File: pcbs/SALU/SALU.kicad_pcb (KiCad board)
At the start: 4 copper layers, 13 parts, among them J201 Conn_02x20_Odd_Even, U201 74HC245, U202 74HC245

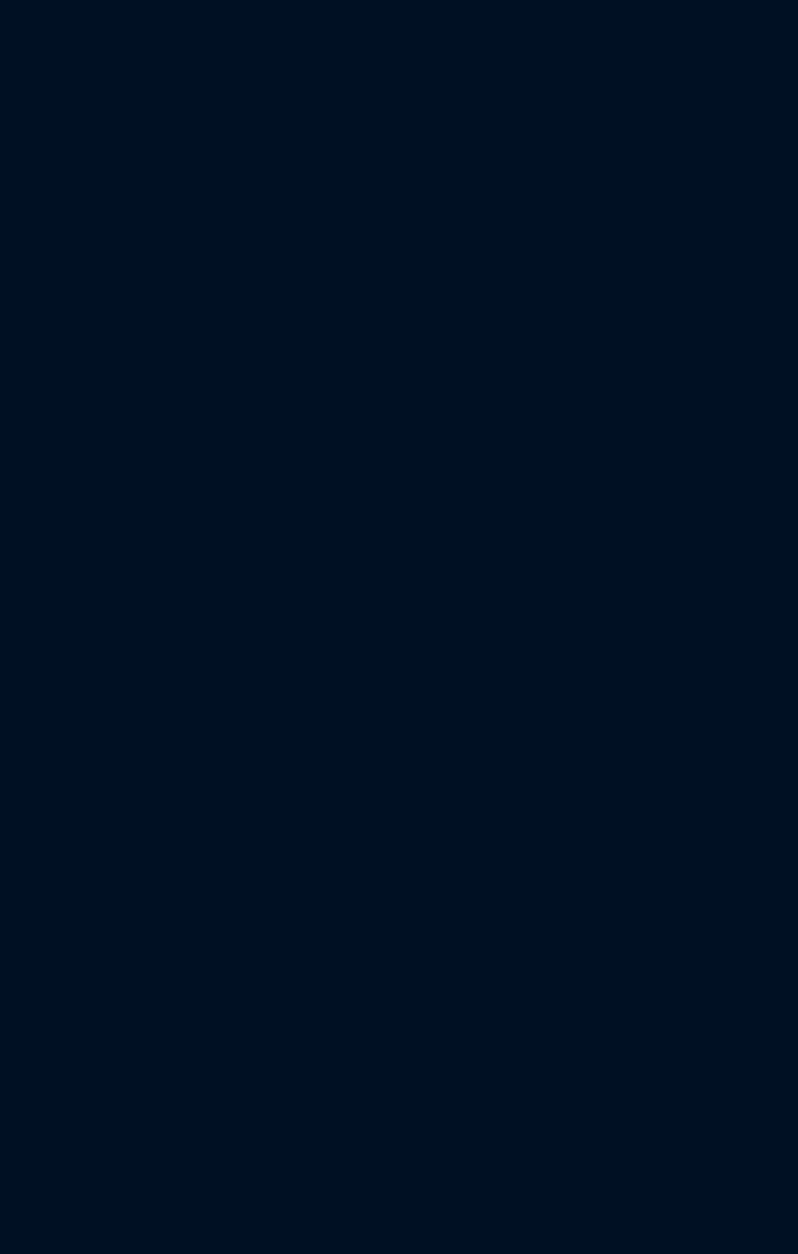
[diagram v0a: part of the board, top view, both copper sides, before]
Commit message: Decoder stage
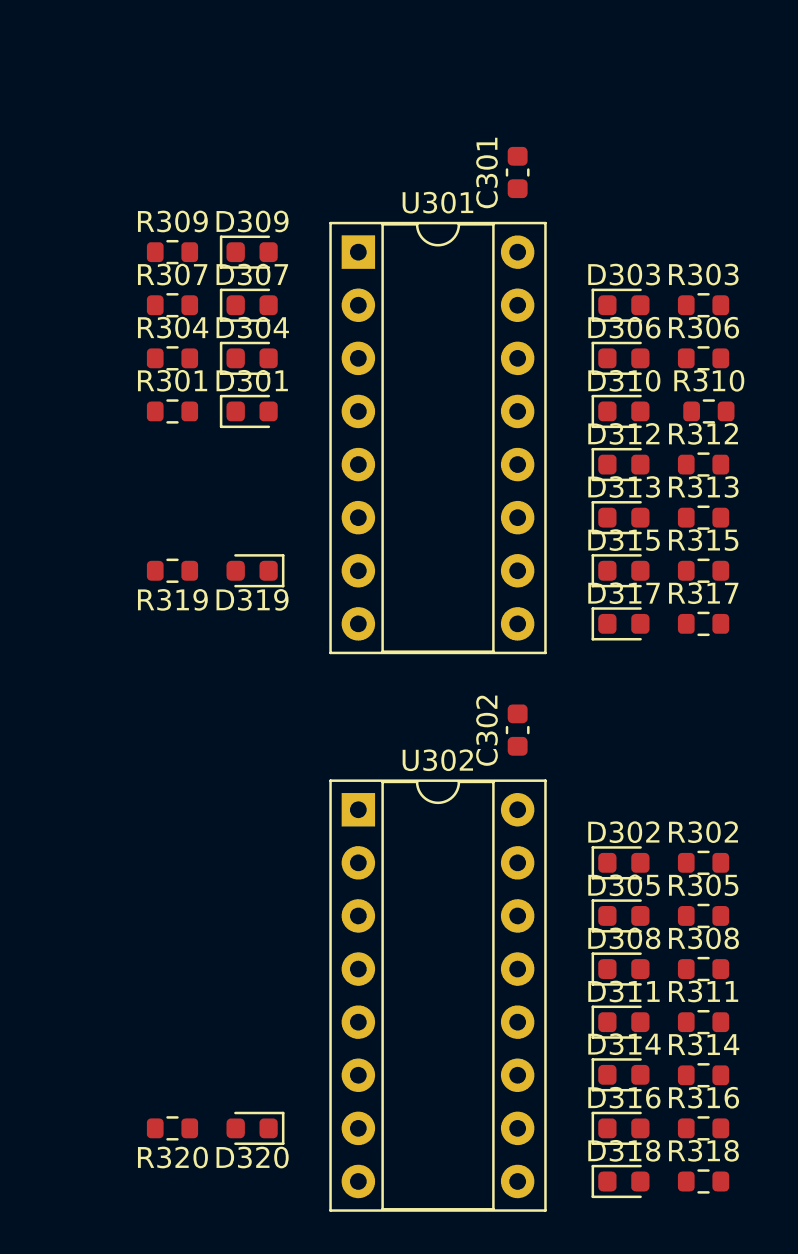
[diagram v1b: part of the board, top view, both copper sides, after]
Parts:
- added C301: 100n, Capacitor_SMD:C_0603_1608Metric, F.Cu at (66.0, 120.7)
- added C302: 100n, Capacitor_SMD:C_0603_1608Metric, F.Cu at (66.0, 147.3)
- added D301: GREEN, LED_SMD:LED_0603_1608Metric, F.Cu at (53.3, 132.1)
- added D302: GREEN, LED_SMD:LED_0603_1608Metric, F.Cu at (71.1, 153.7)
- added D303: GREEN, LED_SMD:LED_0603_1608Metric, F.Cu at (71.1, 127.0)
- added D304: GREEN, LED_SMD:LED_0603_1608Metric, F.Cu at (53.3, 129.5)
- added D305: GREEN, LED_SMD:LED_0603_1608Metric, F.Cu at (71.1, 156.2)
- added D306: GREEN, LED_SMD:LED_0603_1608Metric, F.Cu at (71.1, 129.5)
- added D307: GREEN, LED_SMD:LED_0603_1608Metric, F.Cu at (53.3, 127.0)
- added D308: RED, LED_SMD:LED_0603_1608Metric, F.Cu at (71.1, 158.8)
- added D309: GREEN, LED_SMD:LED_0603_1608Metric, F.Cu at (53.3, 124.5)
- added D310: GREEN, LED_SMD:LED_0603_1608Metric, F.Cu at (71.1, 132.1)
- added D311: RED, LED_SMD:LED_0603_1608Metric, F.Cu at (71.1, 161.3)
- added D312: GREEN, LED_SMD:LED_0603_1608Metric, F.Cu at (71.1, 134.6)
- added D313: RED, LED_SMD:LED_0603_1608Metric, F.Cu at (71.1, 137.2)
- added D314: GREEN, LED_SMD:LED_0603_1608Metric, F.Cu at (71.1, 163.8)
- added D315: RED, LED_SMD:LED_0603_1608Metric, F.Cu at (71.1, 139.7)
- added D316: GREEN, LED_SMD:LED_0603_1608Metric, F.Cu at (71.1, 166.4)
- added D317: RED, LED_SMD:LED_0603_1608Metric, F.Cu at (71.1, 142.2)
- added D318: GREEN, LED_SMD:LED_0603_1608Metric, F.Cu at (71.1, 168.9)
- added D319: RED, LED_SMD:LED_0603_1608Metric, F.Cu at (53.3, 139.7)
- added D320: GREEN, LED_SMD:LED_0603_1608Metric, F.Cu at (53.3, 166.4)
- added R301: 4k7, Resistor_SMD:R_0603_1608Metric, F.Cu at (49.5, 132.1)
- added R302: 4k7, Resistor_SMD:R_0603_1608Metric, F.Cu at (74.9, 153.7)
- added R303: 4k7, Resistor_SMD:R_0603_1608Metric, F.Cu at (74.9, 127.0)
- added R304: 4k7, Resistor_SMD:R_0603_1608Metric, F.Cu at (49.5, 129.5)
- added R305: 4k7, Resistor_SMD:R_0603_1608Metric, F.Cu at (74.9, 156.2)
- added R306: 4k7, Resistor_SMD:R_0603_1608Metric, F.Cu at (74.9, 129.5)
- added R307: 4k7, Resistor_SMD:R_0603_1608Metric, F.Cu at (49.5, 127.0)
- added R308: 4k7, Resistor_SMD:R_0603_1608Metric, F.Cu at (74.9, 158.8)
- added R309: 4k7, Resistor_SMD:R_0603_1608Metric, F.Cu at (49.5, 124.5)
- added R310: 4k7, Resistor_SMD:R_0603_1608Metric, F.Cu at (75.2, 132.1)
- added R311: 4k7, Resistor_SMD:R_0603_1608Metric, F.Cu at (74.9, 161.3)
- added R312: 4k7, Resistor_SMD:R_0603_1608Metric, F.Cu at (74.9, 134.6)
- added R313: 4k7, Resistor_SMD:R_0603_1608Metric, F.Cu at (74.9, 137.2)
- added R314: 4k7, Resistor_SMD:R_0603_1608Metric, F.Cu at (74.9, 163.8)
- added R315: 4k7, Resistor_SMD:R_0603_1608Metric, F.Cu at (74.9, 139.7)
- added R316: 4k7, Resistor_SMD:R_0603_1608Metric, F.Cu at (74.9, 166.4)
- added R317: 4k7, Resistor_SMD:R_0603_1608Metric, F.Cu at (74.9, 142.2)
- added R318: 4k7, Resistor_SMD:R_0603_1608Metric, F.Cu at (74.9, 168.9)
- added R319: 4k7, Resistor_SMD:R_0603_1608Metric, F.Cu at (49.5, 139.7)
- added R320: 4k7, Resistor_SMD:R_0603_1608Metric, F.Cu at (49.5, 166.4)
- added U301: 74HC138, Package_DIP:DIP-16_W7.62mm_Socket, F.Cu at (58.4, 124.5)
- added U302: 74HC138, Package_DIP:DIP-16_W7.62mm_Socket, F.Cu at (58.4, 151.1)

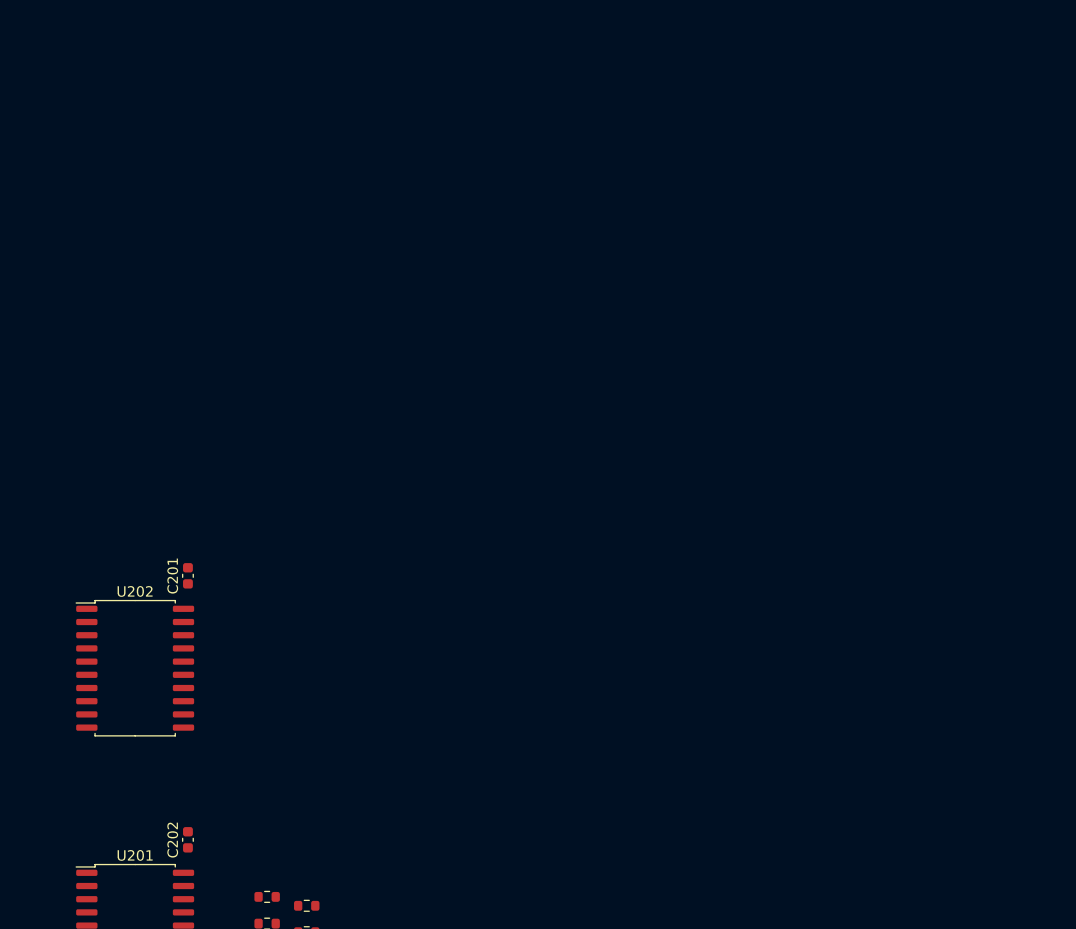
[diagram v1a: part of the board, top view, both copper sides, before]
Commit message: Starting on inc/dec
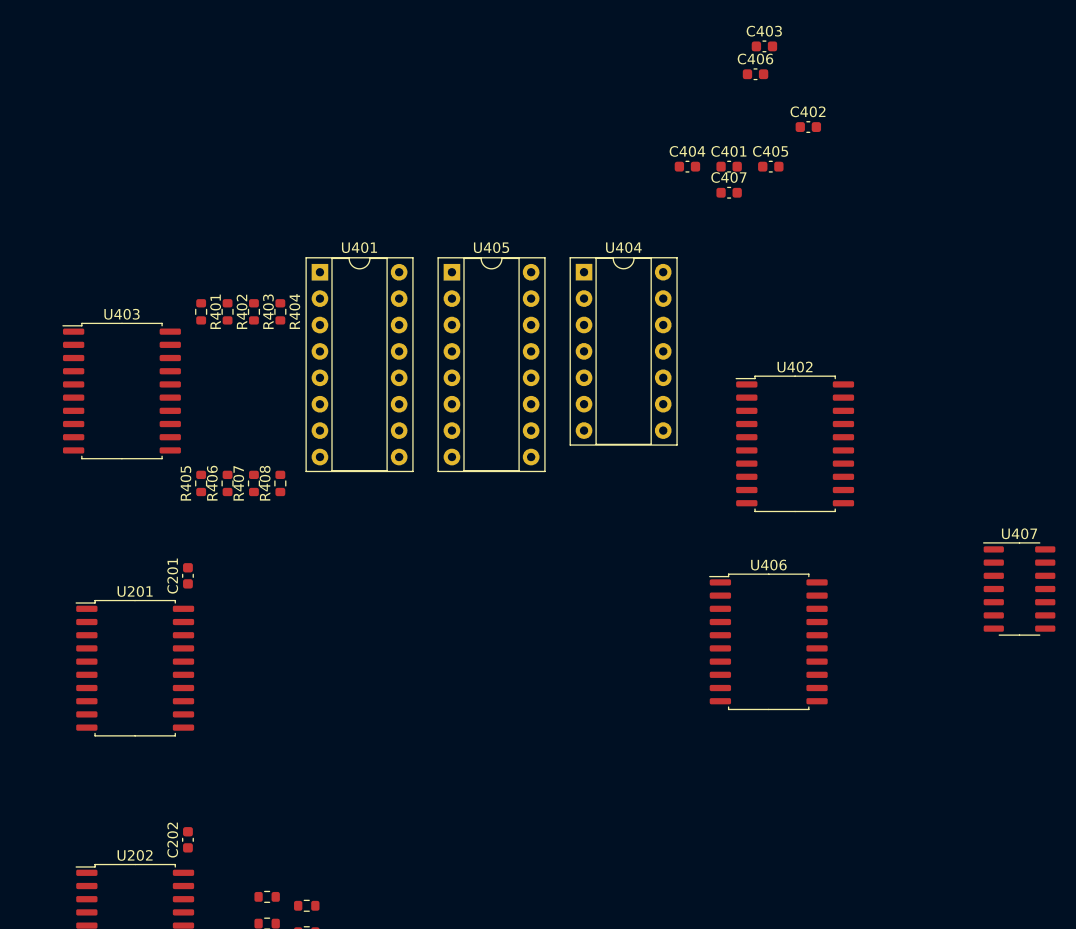
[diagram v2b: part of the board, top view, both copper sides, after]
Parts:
- added C401: 100n, Capacitor_SMD:C_0603_1608Metric, F.Cu at (110.5, 30.5)
- added C402: 100n, Capacitor_SMD:C_0603_1608Metric, F.Cu at (118.1, 26.7)
- added C403: 100n, Capacitor_SMD:C_0603_1608Metric, F.Cu at (113.9, 18.9)
- added C404: 100n, Capacitor_SMD:C_0603_1608Metric, F.Cu at (106.5, 30.5)
- added C405: 100n, Capacitor_SMD:C_0603_1608Metric, F.Cu at (114.5, 30.5)
- added C406: 100n, Capacitor_SMD:C_0603_1608Metric, F.Cu at (113.0, 21.6)
- added C407: 100n, Capacitor_SMD:C_0603_1608Metric, F.Cu at (110.5, 33.0)
- added R401: 220k, Resistor_SMD:R_0603_1608Metric, F.Cu at (59.7, 44.5)
- added R402: 220k, Resistor_SMD:R_0603_1608Metric, F.Cu at (62.2, 44.5)
- added R403: 220k, Resistor_SMD:R_0603_1608Metric, F.Cu at (64.8, 44.5)
- added R404: 220k, Resistor_SMD:R_0603_1608Metric, F.Cu at (67.3, 44.5)
- added R405: 220k, Resistor_SMD:R_0603_1608Metric, F.Cu at (59.7, 61.0)
- added R406: 220k, Resistor_SMD:R_0603_1608Metric, F.Cu at (62.2, 61.0)
- added R407: 220k, Resistor_SMD:R_0603_1608Metric, F.Cu at (64.8, 61.0)
- added R408: 220k, Resistor_SMD:R_0603_1608Metric, F.Cu at (67.3, 61.0)
- added U401: 74HC283, Package_DIP:DIP-16_W7.62mm_Socket, F.Cu at (71.1, 40.6)
- added U402: 74HC245, Package_SO:SOIC-20W_7.5x12.8mm_P1.27mm, F.Cu at (116.8, 57.1)
- added U403: 74HC245, Package_SO:SOIC-20W_7.5x12.8mm_P1.27mm, F.Cu at (52.1, 52.1)
- added U404: 74HC86, Package_DIP:DIP-14_W7.62mm_Socket, F.Cu at (96.5, 40.6)
- added U405: 74HC283, Package_DIP:DIP-16_W7.62mm_Socket, F.Cu at (83.8, 40.6)
- added U406: 74HC245, Package_SO:SOIC-20W_7.5x12.8mm_P1.27mm, F.Cu at (114.3, 76.2)
- added U407: 74HC08, Package_SO:SOIC-14_3.9x8.7mm_P1.27mm, F.Cu at (138.4, 71.1)
- renumbered U202 to U201, U201 to U202

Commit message: Tweaking PCB layout
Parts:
- moved C403 63.3 mm to (57.1, 47.0), turned to 90 degrees
- moved U407 49.3 mm to (110.5, 30.5)
- moved C402 35.8 mm to (108.0, 61.0)
- moved C401 32.6 mm to (78.7, 22.9), turned to 90 degrees
- moved U406 27.9 mm to (100.3, 52.1)
- moved C406 24.7 mm to (108.0, 45.7)
- moved C405 24.3 mm to (91.4, 22.9), turned to 90 degrees
- moved U402 19.4 mm to (100.3, 67.3)
- moved U401 14.0 mm to (71.1, 26.7)
- moved U405 14.0 mm to (83.8, 26.7)
- moved U404 14.0 mm to (96.5, 26.7)
- moved C407 9.21 mm to (113.0, 24.1), turned to 90 degrees
- moved C404 7.96 mm to (104.1, 22.9), turned to 90 degrees
- moved U403 3.81 mm to (52.1, 55.9)
- moved R401 3.81 mm to (59.7, 48.3)
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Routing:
- net /Connector/A4: track 0.00 -> 46.2 mm
- net /Connector/A1: track 0.00 -> 46.2 mm
- net /Connector/A3: track 0.00 -> 46.2 mm
- net /Connector/A7: track 0.00 -> 46.2 mm
- net /Connector/A6: track 0.00 -> 46.2 mm
- net /Connector/A2: track 0.00 -> 46.2 mm
- net /Connector/A0: track 0.00 -> 46.2 mm
- net /Connector/A5: track 0.00 -> 45.9 mm

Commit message: Some more functions
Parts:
- added C501: 100n, Capacitor_SMD:C_0603_1608Metric, F.Cu at (95.2, 94.0)
- added C502: 100n, Capacitor_SMD:C_0603_1608Metric, F.Cu at (98.6, 119.4)
- added C503: 100n, Capacitor_SMD:C_0603_1608Metric, F.Cu at (113.0, 94.0)
- added C504: 100n, Capacitor_SMD:C_0603_1608Metric, F.Cu at (113.0, 135.9)
- added C601: 100n, Capacitor_SMD:C_0603_1608Metric, F.Cu at (134.6, 94.0)
- added C602: 100n, Capacitor_SMD:C_0603_1608Metric, F.Cu at (134.6, 111.8)
- added U501: 74HC00, Package_DIP:DIP-14_W7.62mm_Socket, F.Cu at (87.6, 97.8)
- added U502: 74HC00, Package_DIP:DIP-14_W7.62mm_Socket, F.Cu at (87.6, 119.4)
- added U503: 74HC245, Package_SO:SOIC-20W_7.5x12.8mm_P1.27mm, F.Cu at (108.0, 102.9)
- added U504: 74HC245, Package_SO:SOIC-20W_7.5x12.8mm_P1.27mm, F.Cu at (108.0, 144.8)
- added U601: 74HC245, Package_SO:SOIC-20W_7.5x12.8mm_P1.27mm, F.Cu at (129.5, 102.9)
- added U602: 74HC245, Package_SO:SOIC-20W_7.5x12.8mm_P1.27mm, F.Cu at (129.5, 120.7)
- renumbered D304 to D302, D307 to D303, D309 to D304, D317 to D305, D319 to D306, D313 to D307, D315 to D308, D303 to D309, D306 to D310, D310 to D311, D318 to D313, D320 to D314, D302 to D315, D305 to D316, D308 to D317, D311 to D318, D314 to D319, D316 to D320, R304 to R302, R307 to R303, R309 to R304, R317 to R305, R319 to R306, R303 to R307, R306 to R308, R310 to R309, R312 to R310, R313 to R311, R315 to R312, R318 to R313, R320 to R314, R302 to R315, R305 to R316, R314 to R317, R316 to R318, R308 to R319, R311 to R320, U202 to U201, U201 to U202, U403 to U401, U404 to U402, U407 to U403, U401 to U404, U402 to U406, U406 to U407
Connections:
- net /Connector/A0 renamed /Barrel Shifters/A0
- net /Connector/A1 renamed /Barrel Shifters/A1
- net /Connector/A2 renamed /Barrel Shifters/A2
- net /Connector/A3 renamed /Barrel Shifters/A3
- net /Connector/A4 renamed /Barrel Shifters/A4
- net /Connector/A5 renamed /Barrel Shifters/A5
- net /Connector/A6 renamed /Barrel Shifters/A6
- net /Connector/A7 renamed /Barrel Shifters/A7
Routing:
- net /Barrel Shifters/A5: track 45.9 -> 79.2 mm
- net /Barrel Shifters/A2: track 46.2 -> 79.2 mm
- net /Barrel Shifters/A7: track 46.2 -> 79.2 mm
- net /Barrel Shifters/A6: track 46.2 -> 79.2 mm
- net /Barrel Shifters/A4: track 46.2 -> 79.2 mm
- net /Barrel Shifters/A1: track 46.2 -> 79.2 mm
- net /Barrel Shifters/A0: track 46.2 -> 79.2 mm
- net /Barrel Shifters/A3: track 46.2 -> 79.2 mm

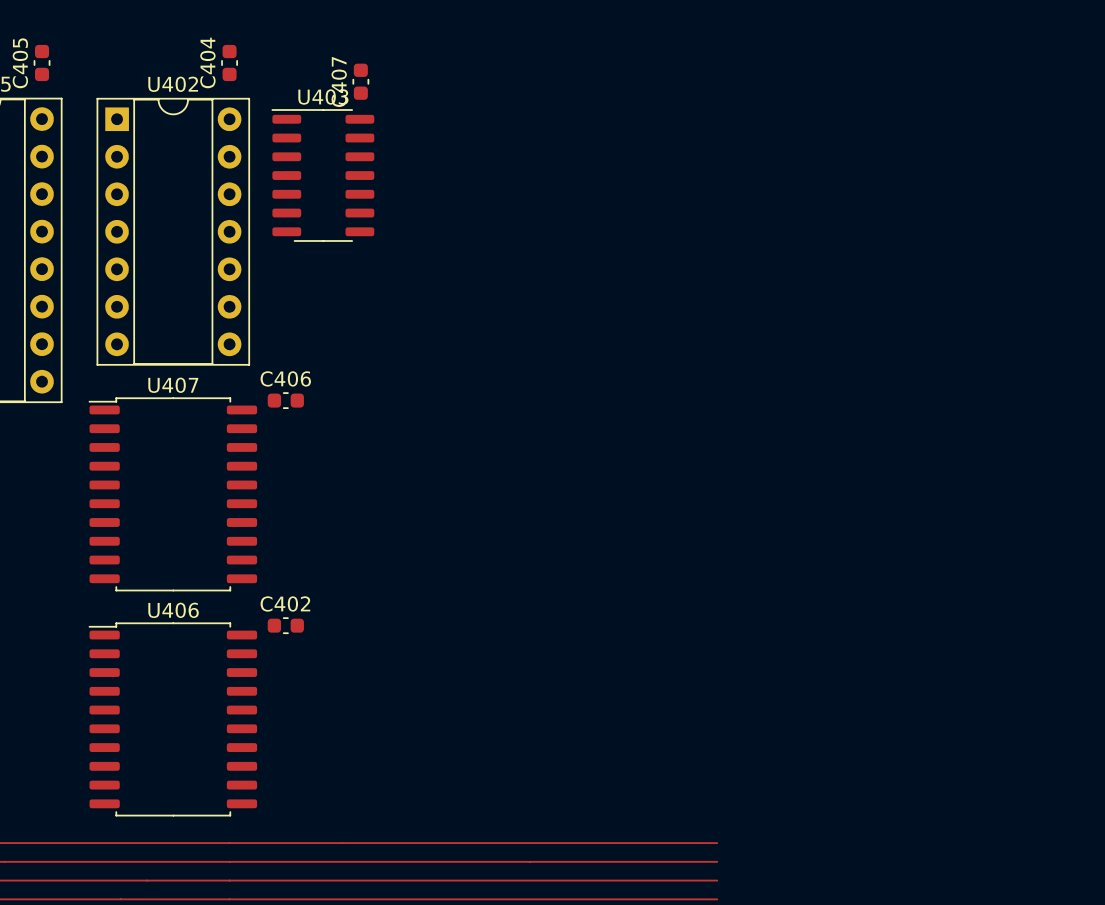
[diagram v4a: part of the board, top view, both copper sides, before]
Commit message: Add shifters
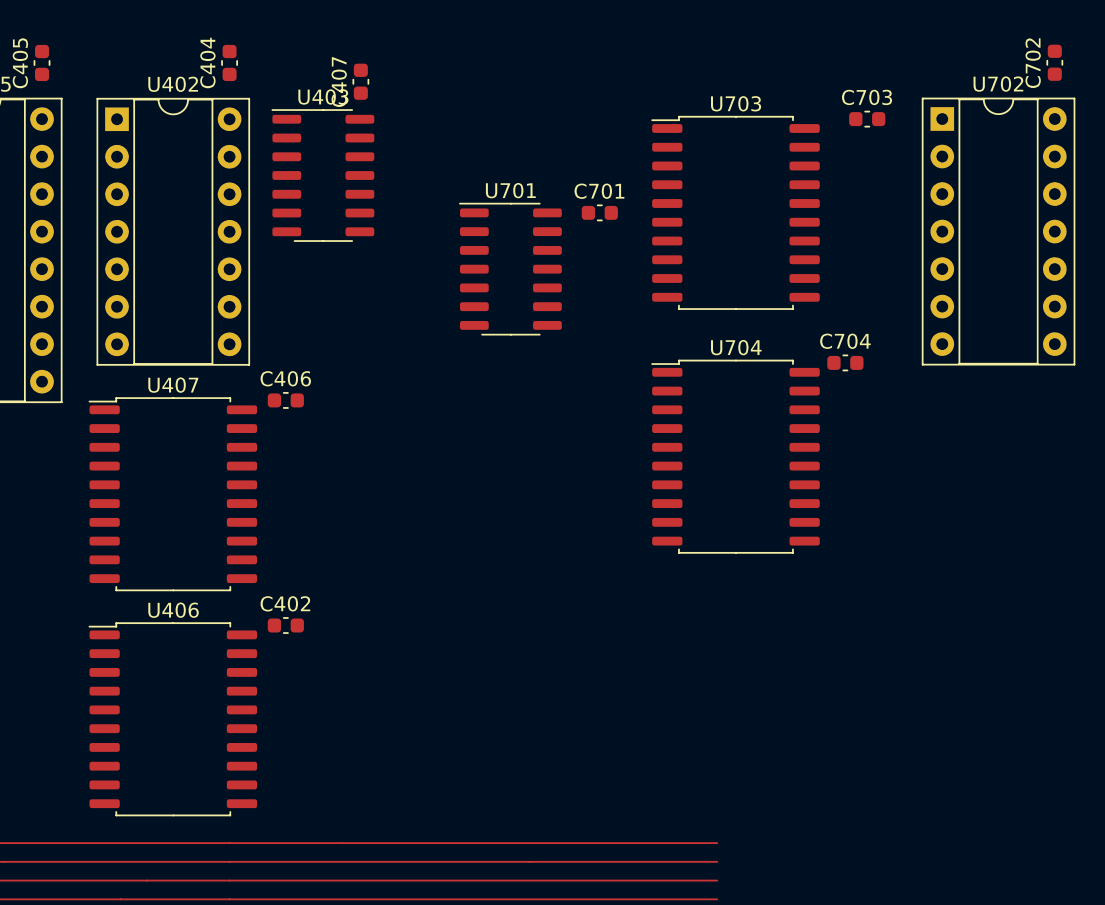
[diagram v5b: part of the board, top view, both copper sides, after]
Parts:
- added C701: 100n, Capacitor_SMD:C_0603_1608Metric, F.Cu at (129.2, 33.0)
- added C702: 100n, Capacitor_SMD:C_0603_1608Metric, F.Cu at (160.0, 22.9)
- added C703: 100n, Capacitor_SMD:C_0603_1608Metric, F.Cu at (147.3, 26.7)
- added C704: 100n, Capacitor_SMD:C_0603_1608Metric, F.Cu at (145.8, 43.2)
- added U701: 74HC08, Package_SO:SOIC-14_3.9x8.7mm_P1.27mm, F.Cu at (123.2, 36.8)
- added U702: 74HCT125, Package_DIP:DIP-14_W7.62mm_Socket, F.Cu at (152.4, 26.7)
- added U703: 74HC245, Package_SO:SOIC-20W_7.5x12.8mm_P1.27mm, F.Cu at (138.4, 33.0)
- added U704: 74HC245, Package_SO:SOIC-20W_7.5x12.8mm_P1.27mm, F.Cu at (138.4, 49.5)
